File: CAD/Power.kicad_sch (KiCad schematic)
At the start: 63 parts, among them U10 AOZ1284, U18 AP7330-W5-7, U24 LM70860RRXR, U4 AP7361C-33E-13

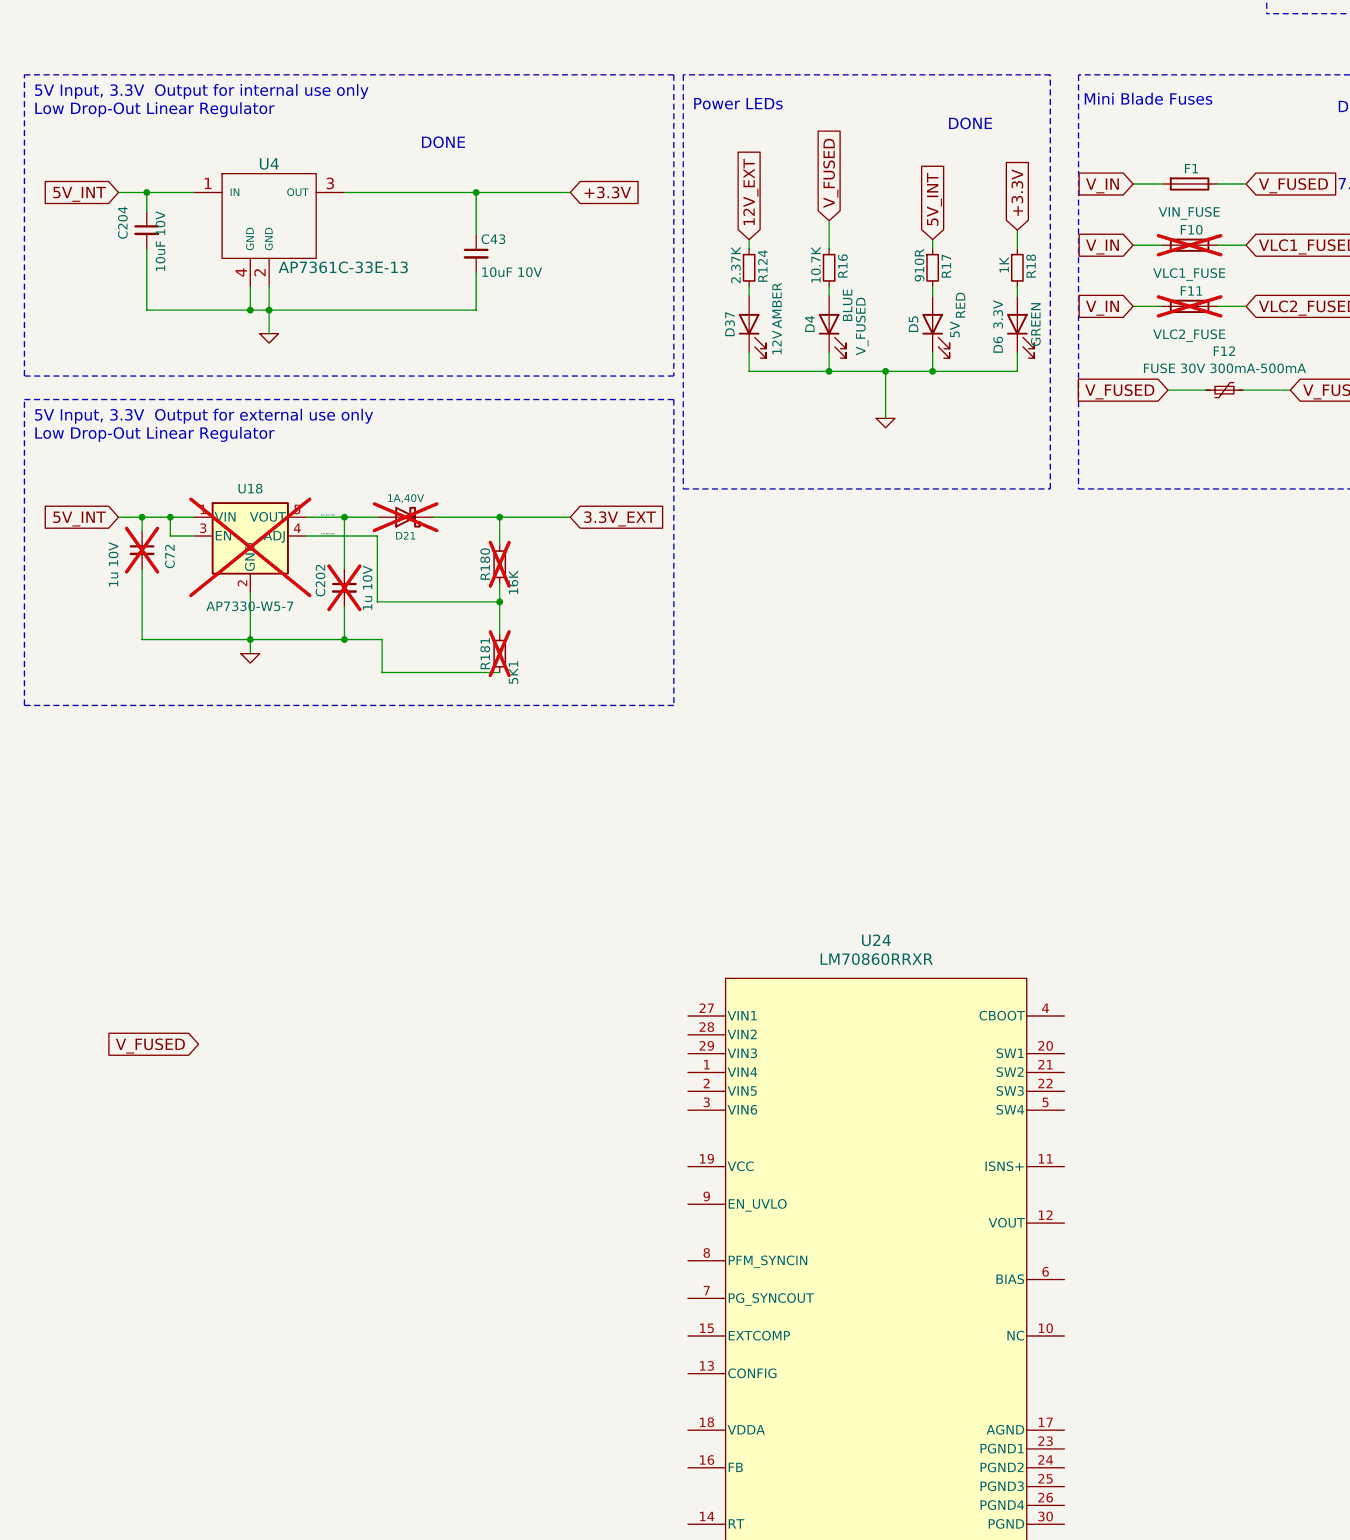
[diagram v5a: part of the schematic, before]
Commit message: Started LM70860
New 5V 6A (built for 4A) buck dc/dc converter, higher range of input voltage (4.5V-80V), built for 12V-75V according to https://webench.ti.com/power-designer/switching-regulator/customize/3?VinMin=12&VinMax=75&O1V=5&O1I=4&base_pn=LM70860-Q1&AppType=None&Flavor=None&op_TA=35&origin=pf_panel&lang_chosen=en-US&optfactor=3&Topology=Buck&flavor=None&VoltageOption=None
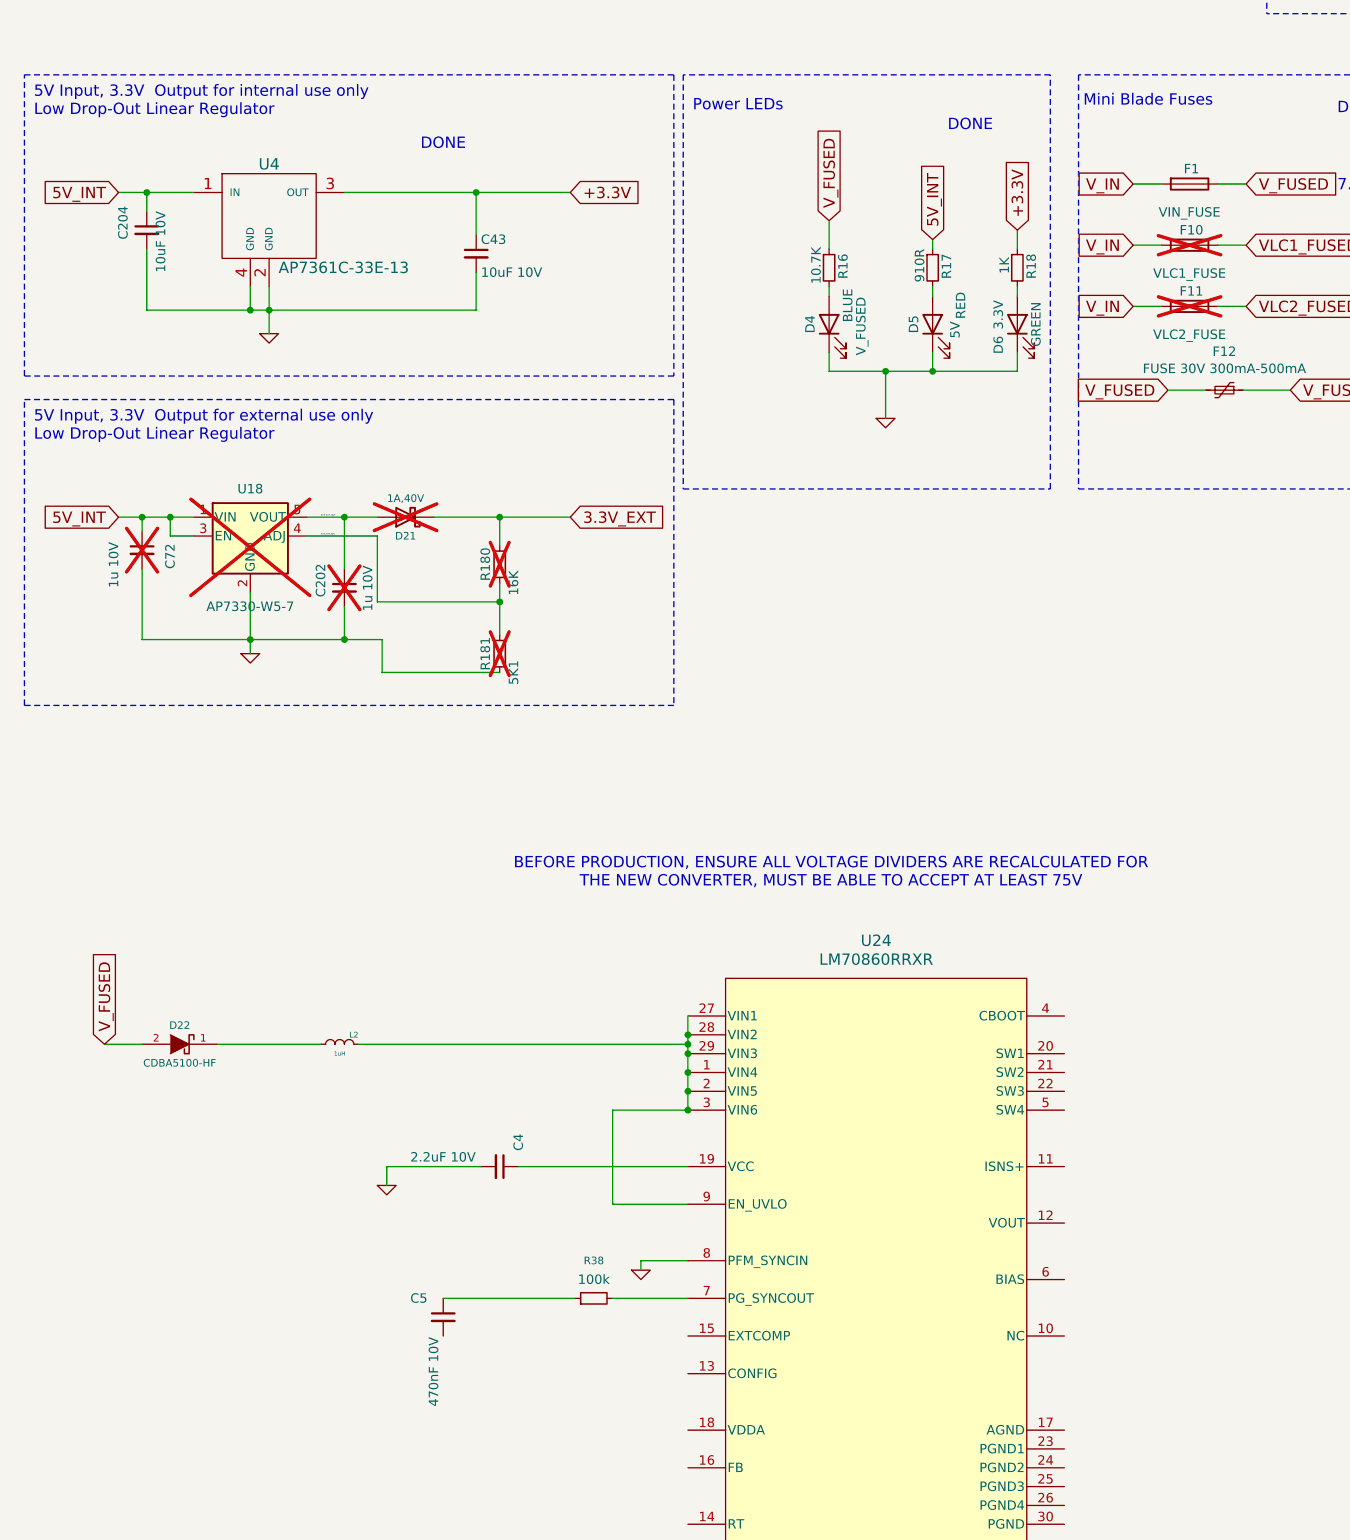
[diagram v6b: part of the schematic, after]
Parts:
- removed D37: AMBER, LED_SMD:LED_0603_1608Metric, symbol Device:LED
- removed R124: 2.37K, Resistor_SMD:R_0402_1005Metric_Wbry, symbol Device:R_Small
- added C4: 2.2uF 10V, Capacitor_SMD:C_0603_1608Metric, symbol Device:C_Small
- added C5: 470nF 10V, Capacitor_SMD:C_0402_1005Metric, symbol Device:C_Small
- added D22: CDBA5100-HF, Diode_SMD:D_SMC, symbol Duet3:CDBA540
- added L2: 1uH, Inductor_SMD:L_1210_3225Metric, symbol Duet3:L_MINI
- added R38: 100k, Resistor_SMD:R_0603_1608Metric, symbol Device:R_Small
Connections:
- net GND: now also U24.8 (PFM_SYNCIN), C4.2
- net V_FUSED: now also D22.2 (A)
- net at U24.1 (VIN4): now also U24.2 (VIN5), U24.27 (VIN1), U24.28 (VIN2), U24.29 (VIN3), U24.3 (VIN6), U24.9 (EN_UVLO), L2.1 (A)
- net at U24.19 (VCC): now also C4.1
- net at U24.7 (PG_SYNCOUT): now also R38.2
- new net: D22.1 (K), L2.2 (B)
- new net: C5.1, R38.1
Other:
- note added: "BEFORE PRODUCTION, ENSURE ALL VOLTAGE DIVIDERS ARE RECALCULATED FOR THE NEW CONVERTER, MUST BE ABLE TO ACCEPT AT LEAST 75V"

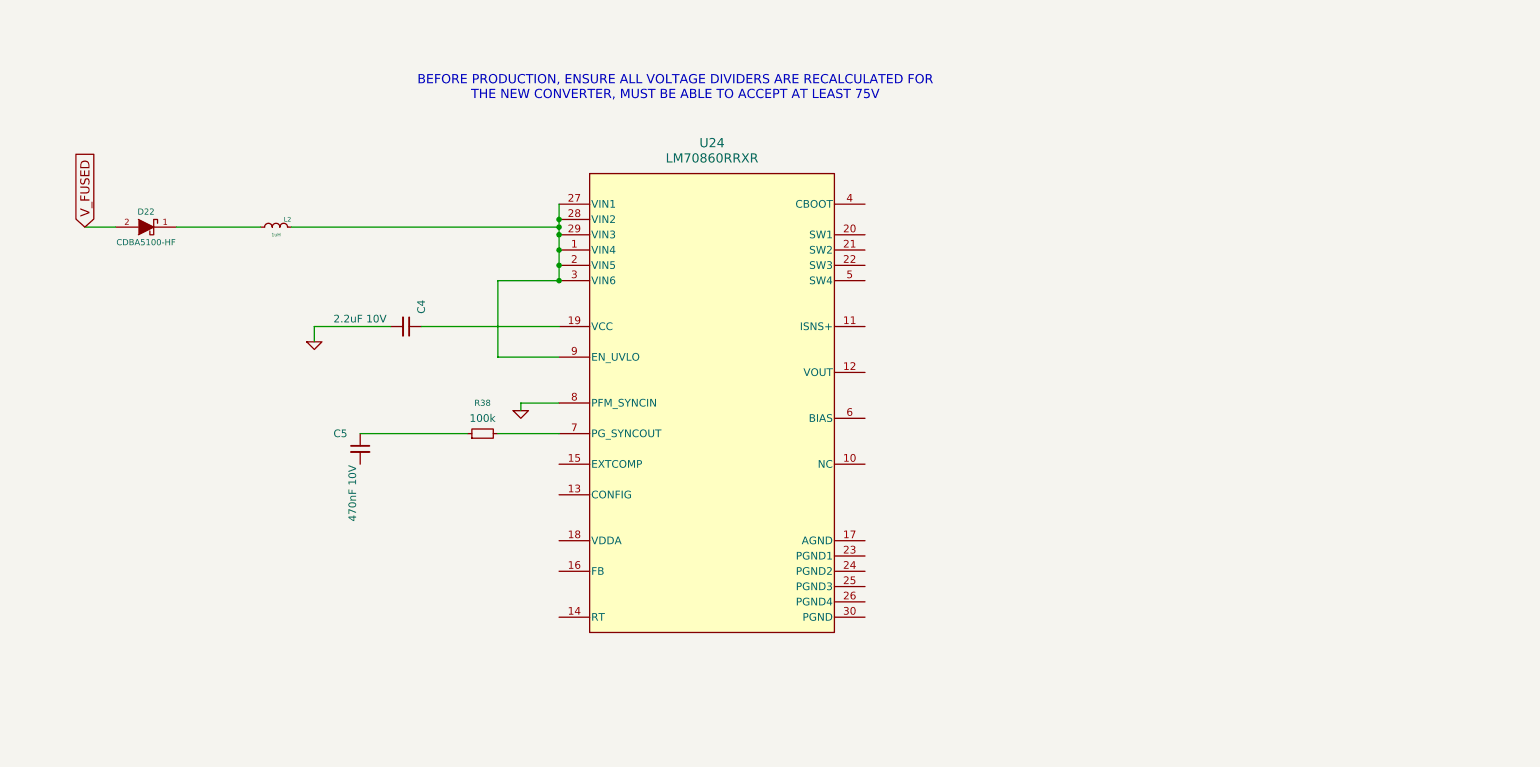
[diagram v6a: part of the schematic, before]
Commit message: LM70860 Components layed out
Still need to connect voltage monitor and make sure all components can handle higher voltage
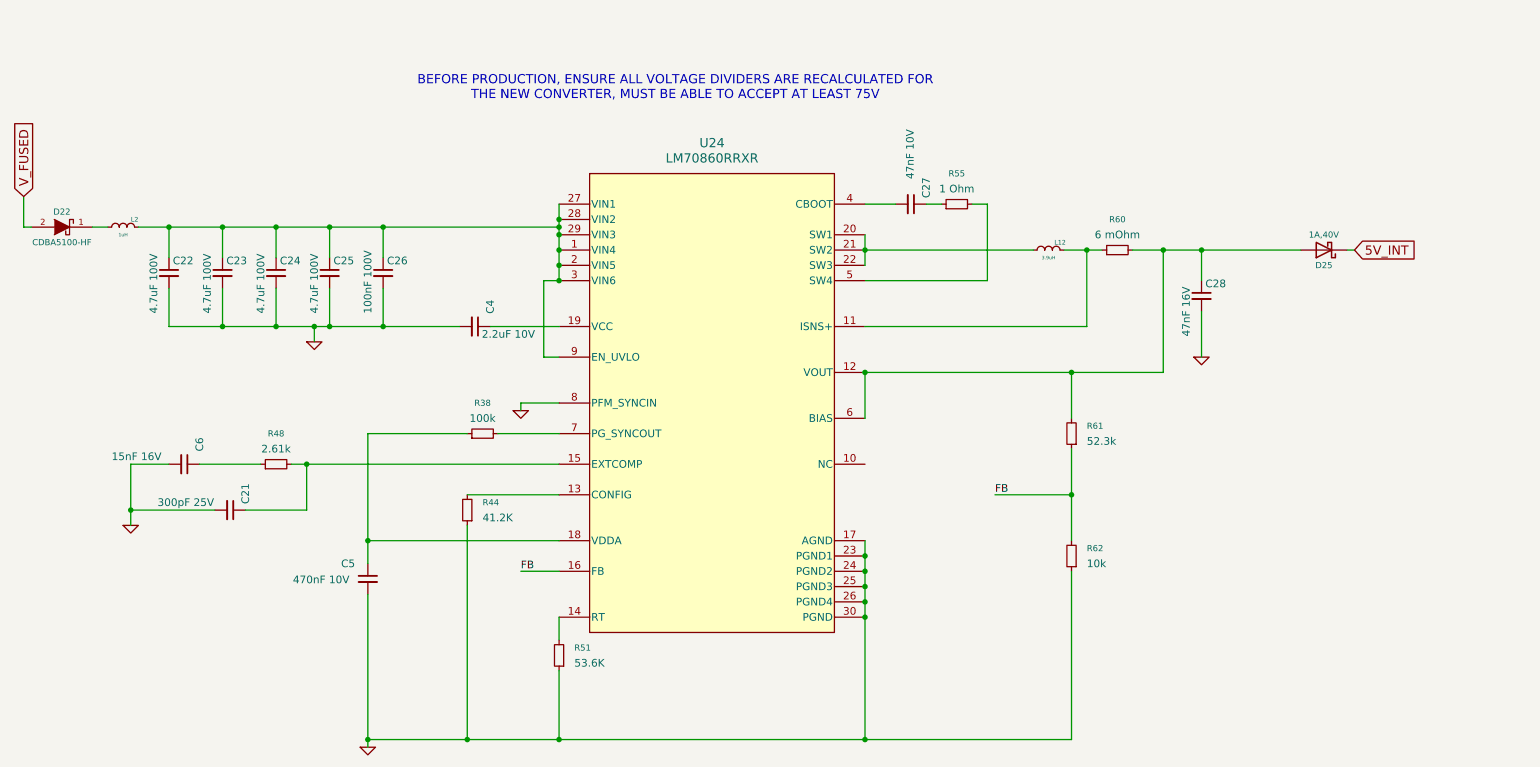
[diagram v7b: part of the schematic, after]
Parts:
- added C21: 300pF 25V, Capacitor_SMD:C_0402_1005Metric, symbol Device:C_Small
- added C22, C23, C24, C25: 4.7uF 100V, Capacitor_SMD:C_1210_3225Metric, symbol Device:C_Small
- added C26: 100nF 100V, Capacitor_SMD:C_0805_2012Metric, symbol Device:C_Small
- added C27: 47nF 10V, Capacitor_SMD:C_0402_1005Metric, symbol Device:C_Small
- added C28: 47nF 16V, Capacitor_SMD:C_1210_3225Metric, symbol Device:C_Small
- added C6: 15nF 16V, Capacitor_SMD:C_0402_1005Metric, symbol Device:C_Small
- added D25: 1A,40V, Diode_SMD:D_SOD-123F, symbol Device:D_Schottky
- added L12: 3.9uH, Inductor_SMD:L_TDK_SLF12575, symbol Duet3:L_MINI
- added R44: 41.2K, Resistor_SMD:R_0603_1608Metric, symbol Device:R_Small
- added R48: 2.61k, Resistor_SMD:R_0402_1005Metric, symbol Device:R_Small
- added R51: 53.6K, Resistor_SMD:R_0603_1608Metric, symbol Device:R_Small
- added R55: 1 Ohm, Resistor_SMD:R_0402_1005Metric, symbol Device:R_Small
- added R60: 6 mOhm, Resistor_SMD:R_0612_1632Metric, symbol Device:R_Small
- added R61: 52.3k, Resistor_SMD:R_0402_1005Metric, symbol Device:R_Small
- added R62: 10k, Resistor_SMD:R_0402_1005Metric, symbol Device:R_Small
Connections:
- net 5V_INT: now also D25.1 (K)
- net GND: now also C5.2, U24.17 (AGND), U24.23 (PGND1), U24.24 (PGND2), U24.25 (PGND3), U24.26 (PGND4), U24.30 (PGND), C21.2, C22.2, C23.2, C24.2, C25.2, C26.2, C28.2, C6.2, R44.1, R51.1, R62.1
- net at L2.1 (A), U24.1 (VIN4), U24.2 (VIN5)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: now also C22.1, C23.1, C24.1, C25.1, C26.1
- net at C5.1, R38.1: now also U24.18 (VDDA)
- net at U24.11 (ISNS+): now also L12.1 (A), R60.1
- net at U24.12 (VOUT): now also U24.6 (BIAS), C28.1, D25.2 (A), R60.2, R61.2
- net at U24.13 (CONFIG): now also R44.2
- net at U24.14 (RT): now also R51.2
- net at U24.15 (EXTCOMP): now also C21.1, R48.2
- net FB: now reaches U24.16 (FB)
- net FB: now also R61.1, R62.2
- net at U24.20 (SW1): now also U24.21 (SW2), U24.22 (SW3), L12.2 (B)
- net at U24.4 (CBOOT): now also C27.2
- net at U24.5 (SW4): now also R55.2
- new net: C27.1, R55.1
- new net: C6.1, R48.1
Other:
- moved on the sheet: C4, C5, D22, L2
